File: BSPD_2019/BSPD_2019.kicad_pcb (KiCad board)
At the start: 2 copper layers, 70.2 x 44 mm, 73 parts, among them J1 MX120G, J2 Override, Q1 BSS84, Q2 BSS84, Q3 BSS84, Q4 NPN, Q5 PNP, Q6 BSS84, U1 LM393ADR, U2 LM393ADR, U3 NCP1117ST50T3G, U4 NAND GATE, U5 AND, U6 NOR GATE

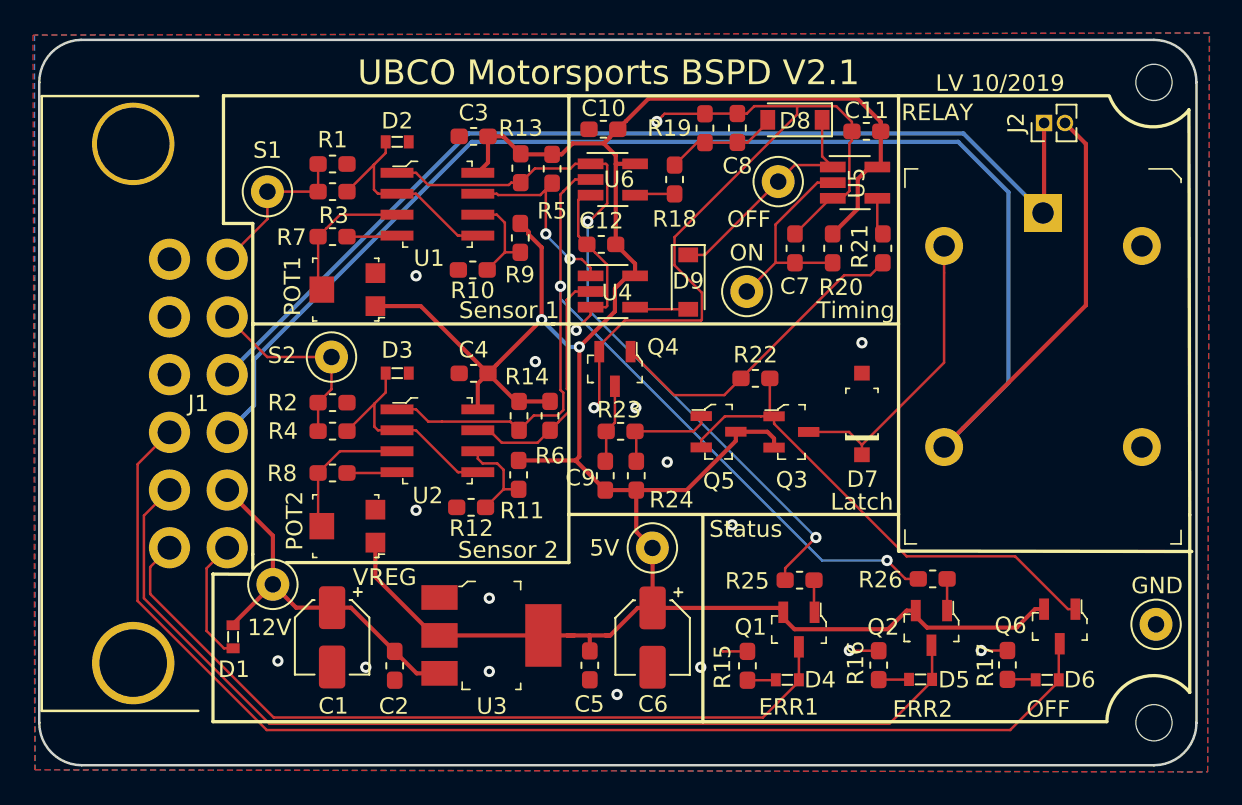
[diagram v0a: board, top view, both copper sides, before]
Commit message: Fixed ESD diode footprints
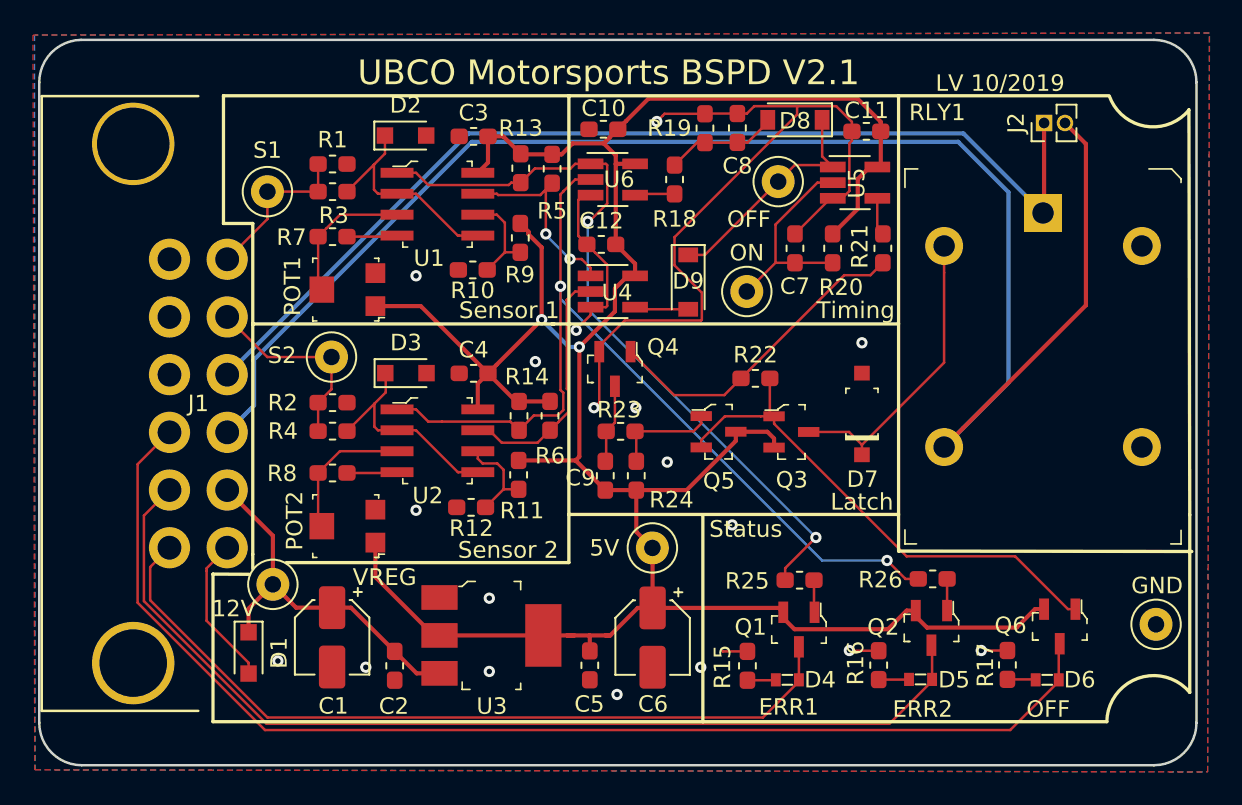
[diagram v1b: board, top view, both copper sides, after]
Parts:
- removed REF** (x2): MountingHole_2.2mm_M2, MountingHole:MountingHole_2.2mm_M2
- D1, D2, D3: footprint digikey-footprints:0603 -> Diode_SMD:D_SOD-323_HandSoldering
- R15, R16, R17: value 100 -> 220
- U3: value NCP1117ST50T3G -> LM1117MPX-5.0
- moved D1 1.36 mm to (113.8, 114.2)
- moved D2 0.63 mm to (123.3, 82.8)
- moved D3 0.53 mm to (123.3, 97.2)
- renumbered RELAY to RLY1
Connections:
- J1 pad 13: GND -> (no net)
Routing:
- net GND: track 78.3 -> 79.8 mm

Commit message: V2.2
Modifications to logic replacing the previous multi-diode layout to a logical OR gate. Changed VREG to a novalithic part with a different footprint
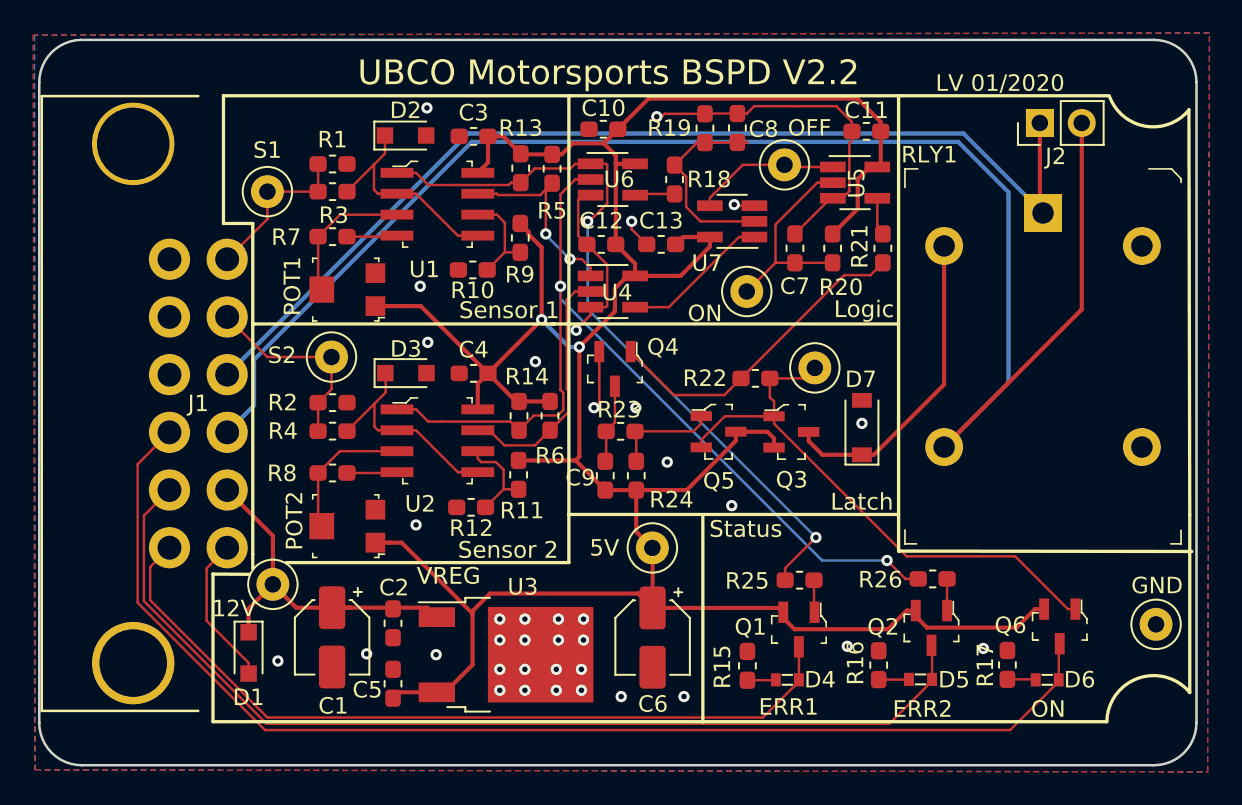
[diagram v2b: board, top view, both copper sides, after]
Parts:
- removed D8, D9: 1N4148W, Diode_SMD:D_SOD-123
- added C13: 100n, Capacitor_SMD:C_0603_1608Metric_Pad1.05x0.95mm_HandSolder, F.Cu at (138.8, 89.4)
- added TP8: Latch TP, TestPoint:TestPoint_Loop_D2.50mm_Drill1.0mm_LowProfile, F.Cu at (148.1, 96.9)
- added U7: OR GATE, Package_TO_SOT_SMD:SOT-23-5_HandSoldering, F.Cu at (143.1, 88.0)
- D7: footprint digikey-footprints:SOD-123 -> Diode_SMD:D_SOD-123
- J2: footprint Connector_PinHeader_1.27mm:PinHeader_1x02_P1.27mm_Vertical -> Connector_PinHeader_2.54mm:PinHeader_1x02_P2.54mm_Vertical
- U3: value LM1117MPX-5.0 -> NCV7805BDTRKG; footprint digikey-footprints:SOT-223 -> Package_TO_SOT_SMD:TO-252-3_TabPin4
- moved C5 12.0 mm to (122.6, 116.1), turned to 270 degrees
- moved C2 2.58 mm to (122.6, 112.4)
- moved U3 1.47 mm to (129.4, 114.3), turned to 0 degrees
- moved TP6 1.09 mm to (146.3, 84.6)
- moved D7 0.83 mm to (151.0, 100.5)
- moved J2 0.25 mm to (161.8, 82.0)
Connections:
- net ERR_OUT renamed ON_OUT
- Q3 pad 3: Net-(D7-PadK) -> Relay_Supply
- RLY1 pad 2: Net-(D7-PadK) -> Relay_Supply
- U3 pad 1: GND -> +12V
- U3 pad 2: +5V -> (no net)
- U3 pad 3: +12V -> +5V
- U3 pad 4: +5V -> GND
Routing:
- net GND: track 79.8 -> 54.3 mm, vias 18 -> 37
- net Relay_Supply: track 0.00 -> 19.3 mm
- net Net-(D7-PadK): track 18.3 -> 0.00 mm
- net +5V: track 164.9 -> 179.9 mm
- net Net-(U4-Pad4): track 3.27 -> 9.00 mm
- net Net-(C8-Pad1): track 6.88 -> 12.3 mm
- net Net-(TP6-Pad1): track 14.2 -> 8.82 mm
- net RELAY: track 31.3 -> 34.3 mm
- net RELAY_O: track 98.1 -> 97.2 mm
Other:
- board text added: "LV 01/2020"
- board text added: "Logic"
- board text added: "UBCO Motorsports BSPD V2.2"
- board text removed: "LV 10/2019"
- board text removed: "Timing"
- board text removed: "UBCO Motorsports BSPD V2.1"

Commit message: Some small changes
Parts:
- added C14: 100n, Capacitor_SMD:C_0603_1608Metric_Pad1.05x0.95mm_HandSolder, F.Cu at (123.4, 81.3)
- added C15: 100n, Capacitor_SMD:C_0603_1608Metric_Pad1.05x0.95mm_HandSolder, F.Cu at (123.3, 95.7)
- C7: value 10u -> 22u
- D2, D3: value ESD Diode -> TVS
- R18: value 30k -> 70k
- R20: value 80k -> 100k
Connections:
- U3 pad 2: (no net) -> GND
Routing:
- net GND: track 54.3 -> 57.6 mm, vias 37 -> 40
- net Net-(C14-Pad2): track 14.0 -> 15.7 mm
- net Net-(C15-Pad2): track 14.0 -> 15.7 mm
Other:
- board text added: "UBCO Motorsports BSPD V2.3"
- board text removed: "UBCO Motorsports BSPD V2.2"
